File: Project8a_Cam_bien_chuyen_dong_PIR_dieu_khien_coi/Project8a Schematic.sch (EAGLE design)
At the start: 6 parts, among them U1 ARDUINOR3-BPLACE

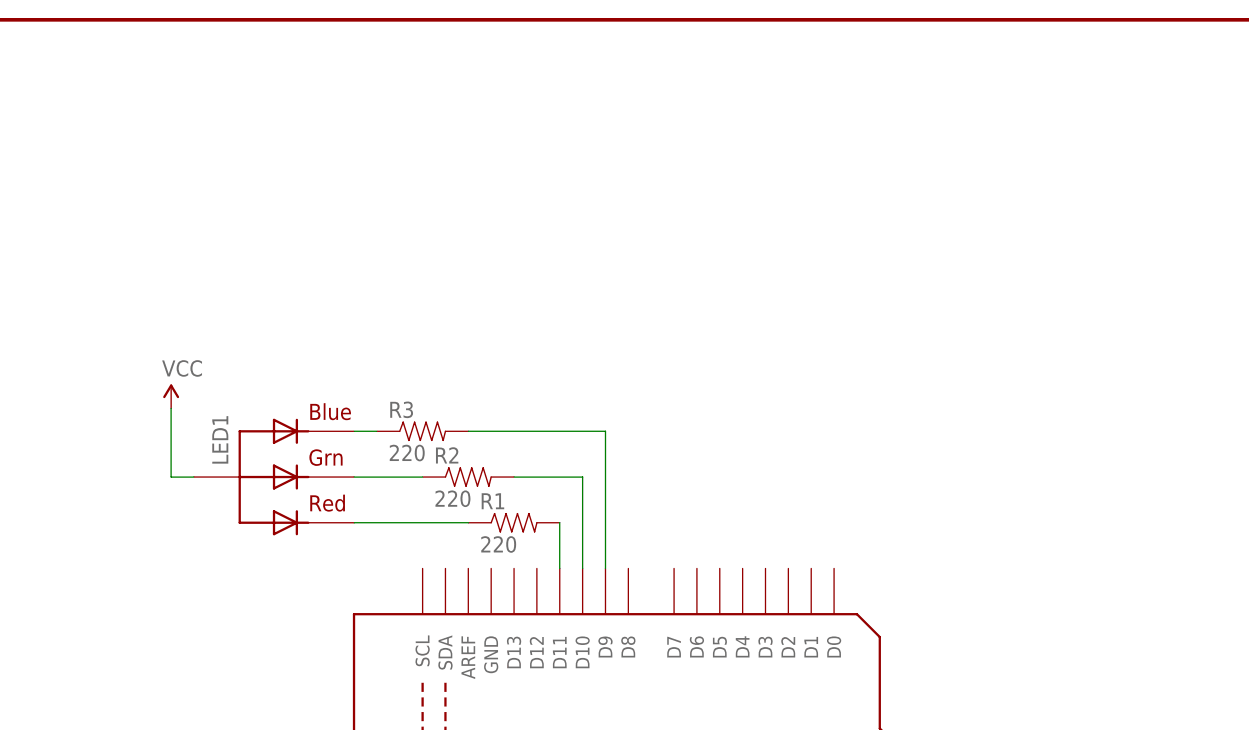
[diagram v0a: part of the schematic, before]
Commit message: Update schematic, breadboard cho nhieu projects.
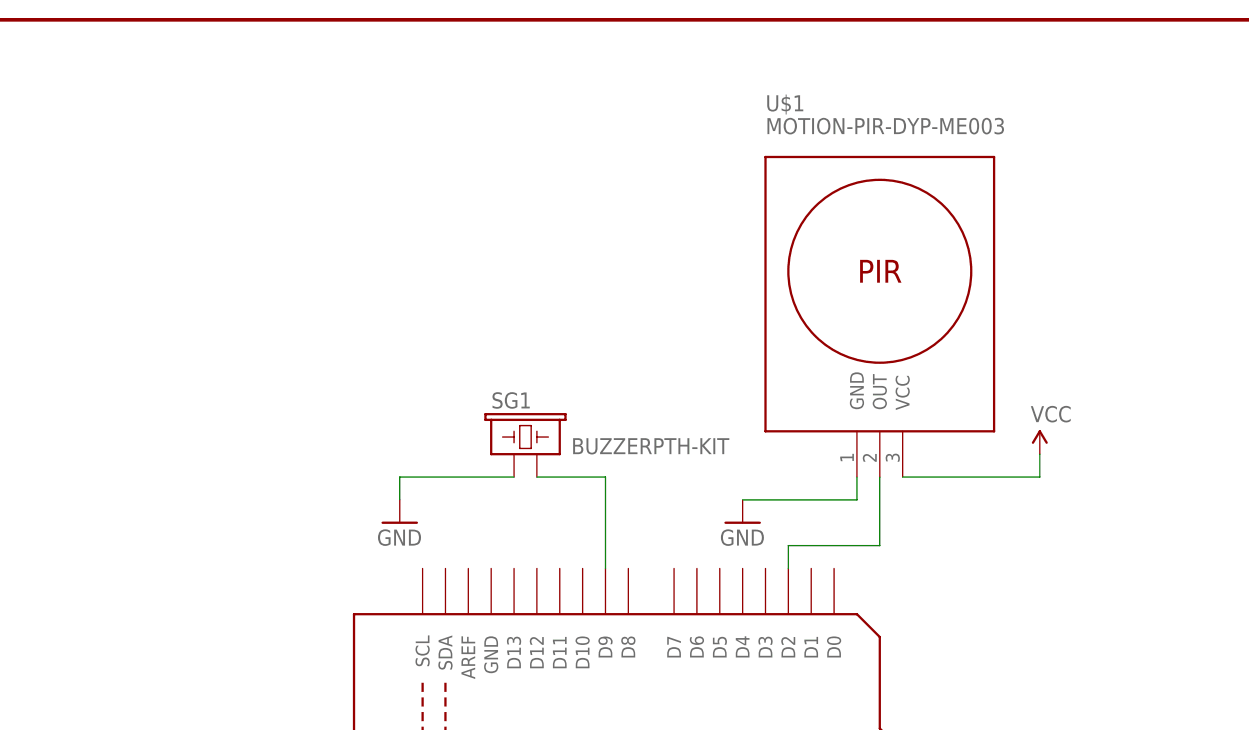
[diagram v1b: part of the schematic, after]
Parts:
- removed LED1: RGBLED_CA-5MM, adafruit:RGBLED_CA-5MM
- removed R1, R2, R3: 220, SparkFun-Passives:RESISTOR0402-RES
- added SG1: BUZZERPTH-KIT, SparkFun-Electromechanical:BUZZERPTH-KIT
- added U$1: MOTION-PIR-DYP-ME003, diy-modules:MOTION-PIR-DYP-ME003
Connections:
- removed net N$2: R2.2, U1.D10
- removed net N$4: LED1.BLUE, R3.1
- removed net N$5: LED1.GREEN, R2.1
- removed net N$6: LED1.RED, R1.1
- net GND: now also SG1.1, U$1.GND
- net N$1: now also SG1.2, U1.D9; no longer R1.2, U1.D11
- net N$3: now also U$1.OUT, U1.D2; no longer R3.2, U1.D9
- net VCC: now also U$1.VCC; no longer LED1.VCC
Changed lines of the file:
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@@
 <layer number="223" name="223bmp" color="24" fill="1" visible="no" active="no"/>
 <layer number="224" name="224bmp" color="25" fill="1" visible="no" active="no"/>
+<layer number="225" name="225bmp" color="7" fill="1" visible="yes" active="yes"/>
+<layer number="226" name="226bmp" color="7" fill="1" visible="yes" active="yes"/>
+<layer number="227" name="227bmp" color="7" fill="1" visible="yes" active="yes"/>
+<layer number="228" name="228bmp" color="7" fill="1" visible="yes" active="yes"/>
+<layer number="229" name="229bmp" color="7" fill="1" visible="yes" active="yes"/>
+<layer number="230" name="230bmp" color="7" fill="1" visible="yes" active="yes"/>
 <layer number="231" name="Eagle3D_PG1" color="7" fill="1" visible="no" active="no"/>
 <layer number="232" name="Eagle3D_PG2" color="7" fill="1" visible="no" active="no"/>
@@
 <part name="SUPPLY1" library="SparkFun-Aesthetics" deviceset="VCC" device=""/>
 <part name="GND1" library="SparkFun-Aesthetics" deviceset="GND" device=""/>
-<part name="R1" library="SparkFun-Passives" deviceset="RESISTOR" device="0402-RES" value="220"/>
+<part name="GND2" library="SparkFun-Aesthetics" deviceset="GND" device=""/>
+<part name="GND3" library="SparkFun-Aesthetics" deviceset="GND" device=""/>
+<part name="SUPPLY2" library="SparkFun-Aesthetics" deviceset="VCC" device=""/>
 <part name="FRAME1" library="SparkFun-Aesthetics" deviceset="FRAME-LETTER" device=""/>
-<part name="LED1" library="adafruit" deviceset="RGBLED_CA" device="-5MM"/>
-<part name="SUPPLY3" library="SparkFun-Aesthetics" deviceset="VCC" device=""/>
-<part name="R2" library="SparkFun-Passives" deviceset="RESISTOR" device="0402-RES" value="220"/>
-<part name="R3" library="SparkFun-Passives" deviceset="RESISTOR" device="0402-RES" value="220"/>
+<part name="U$1" library="diy-modules" deviceset="MOTION-PIR-DYP-ME003" device=""/>
+<part name="SG1" library="SparkFun-Electromechanical" deviceset="BUZZER" device="PTH-KIT"/>
 </parts>
 <sheets>
@@
 <instance part="SUPPLY1" gate="G$1" x="76.2" y="43.18" rot="R180"/>
 <instance part="GND1" gate="1" x="81.28" y="40.64"/>
-<instance part="R1" gate="G$1" x="63.5" y="114.3"/>
+<instance part="GND2" gate="1" x="50.8" y="114.3"/>
+<instance part="GND3" gate="1" x="88.9" y="114.3"/>
+<instance part="SUPPLY2" gate="G$1" x="121.92" y="121.92"/>
 <instance part="FRAME1" gate="G$1" x="-33.02" y="-15.24"/>
 <instance part="FRAME1" gate="V" x="114.3" y="-15.24"/>
-<instance part="LED1" gate="G$1" x="38.1" y="119.38"/>
-<instance part="SUPPLY3" gate="G$1" x="25.4" y="127"/>
-<instance part="R2" gate="G$1" x="58.42" y="119.38"/>
-<instance part="R3" gate="G$1" x="53.34" y="124.46"/>
+<instance part="U$1" gate="G$1" x="104.14" y="139.7"/>
+<instance part="SG1" gate="G$1" x="63.5" y="121.92"/>
 </instances>
 <busses>
@@
 </segment>
 <segment>
-<pinref part="SUPPLY3" gate="G$1" pin="VCC"/>
-<wire x1="25.4" y1="127" x2="25.4" y2="119.38" width="0.1524" layer="91"/>
-<pinref part="LED1" gate="G$1" pin="VCC"/>
-<wire x1="25.4" y1="119.38" x2="27.94" y2="119.38" width="0.1524" layer="91"/>
+<pinref part="U$1" gate="G$1" pin="VCC"/>
+<pinref part="SUPPLY2" gate="G$1" pin="VCC"/>
+<wire x1="106.68" y1="119.38" x2="121.92" y2="119.38" width="0.1524" layer="91"/>
+<wire x1="121.92" y1="119.38" x2="121.92" y2="121.92" width="0.1524" layer="91"/>
 </segment>
 </net>
@@
 <wire x1="81.28" y1="48.26" x2="81.28" y2="43.18" width="0.1524" layer="91"/>
 </segment>
-</net>
-<net name="N$1" class="0">
 <segment>
-<pinref part="U1" gate="G$1" pin="D11"/>
-<wire x1="68.58" y1="114.3" x2="68.58" y2="109.22" width="0.1524" layer="91"/>
-<pinref part="R1" gate="G$1" pin="2"/>
+<pinref part="GND3" gate="1" pin="GND"/>
+<pinref part="U$1" gate="G$1" pin="GND"/>
+<wire x1="88.9" y1="116.84" x2="101.6" y2="116.84" width="0.1524" layer="91"/>
+<wire x1="101.6" y1="116.84" x2="101.6" y2="119.38" width="0.1524" layer="91"/>
 </segment>
-</net>
-<net name="N$2" class="0">
 <segment>
-<pinref part="U1" gate="G$1" pin="D10"/>
-<wire x1="71.12" y1="119.38" x2="71.12" y2="109.22" width="0.1524" layer="91"/>
-<pinref part="R2" gate="G$1" pin="2"/>
-<wire x1="71.12" y1="119.38" x2="63.5" y2="119.38" width="0.1524" layer="91"/>
+<pinref part="SG1" gate="G$1" pin="1"/>
+<wire x1="63.5" y1="119.38" x2="50.8" y2="119.38" width="0.1524" layer="91"/>
+<pinref part="GND2" gate="1" pin="GND"/>
+<wire x1="50.8" y1="119.38" x2="50.8" y2="116.84" width="0.1524" layer="91"/>
 </segment>
 </net>
 <net name="N$3" class="0">
 <segment>
-<pinref part="U1" gate="G$1" pin="D9"/>
-<wire x1="73.66" y1="124.46" x2="73.66" y2="109.22" width="0.1524" layer="91"/>
-<pinref part="R3" gate="G$1" pin="2"/>
-<wire x1="58.42" y1="124.46" x2="73.66" y2="124.46" width="0.1524" layer="91"/>
+<pinref part="U$1" gate="G$1" pin="OUT"/>
+<wire x1="104.14" y1="119.38" x2="104.14" y2="111.76" width="0.1524" layer="91"/>
+<wire x1="104.14" y1="111.76" x2="93.98" y2="111.76" width="0.1524" layer="91"/>
+<pinref part="U1" gate="G$1" pin="D2"/>
+<wire x1="93.98" y1="111.76" x2="93.98" y2="109.22" width="0.1524" layer="91"/>
 </segment>
 </net>
-<net name="N$4" class="0">
+<net name="N$1" class="0">
 <segment>
-<pinref part="LED1" gate="G$1" pin="BLUE"/>
-<pinref part="R3" gate="G$1" pin="1"/>
-<wire x1="45.72" y1="124.46" x2="48.26" y2="124.46" width="0.1524" layer="91"/>
+<pinref part="U1" gate="G$1" pin="D9"/>
+<wire x1="73.66" y1="109.22" x2="73.66" y2="119.38" width="0.1524" layer="91"/>
+<pinref part="SG1" gate="G$1" pin="2"/>
+<wire x1="73.66" y1="119.38" x2="66.04" y2="119.38" width="0.1524" layer="91"/>
 </segment>
 </net>
-<net name="N$5" class="0">
-<segment>
-<pinref part="LED1" gate="G$1" pin="GREEN"/>
-<pinref part="R2" gate="G$1" pin="1"/>
-<wire x1="45.72" y1="119.38" x2="53.34" y2="119.38" width="0.1524" layer="91"/>
-</segment>
-</net>
-<net name="N$6" class="0">
-<segment>
-<pinref part="LED1" gate="G$1" pin="RED"/>
-<pinref part="R1" gate="G$1" pin="1"/>
-<wire x1="45.72" y1="114.3" x2="58.42" y2="114.3" width="0.1524" layer="91"/>
-</segment>
-</net>

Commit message: Thay doi schematic cua projects.
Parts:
- renumbered U$1 to U2
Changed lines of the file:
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@@
 <?xml version="1.0" encoding="utf-8"?>
 <!DOCTYPE eagle SYSTEM "eagle.dtd">
-<eagle version="7.2.0">
+<eagle version="7.3.0">
 <drawing>
 <settings>
@@
 <part name="SUPPLY2" library="SparkFun-Aesthetics" deviceset="VCC" device=""/>
 <part name="FRAME1" library="SparkFun-Aesthetics" deviceset="FRAME-LETTER" device=""/>
-<part name="U$1" library="diy-modules" deviceset="MOTION-PIR-DYP-ME003" device=""/>
+<part name="U2" library="diy-modules" deviceset="MOTION-PIR-DYP-ME003" device=""/>
 <part name="SG1" library="SparkFun-Electromechanical" deviceset="BUZZER" device="PTH-KIT"/>
 </parts>
@@
 <instance part="FRAME1" gate="G$1" x="-33.02" y="-15.24"/>
 <instance part="FRAME1" gate="V" x="114.3" y="-15.24"/>
-<instance part="U$1" gate="G$1" x="104.14" y="139.7"/>
+<instance part="U2" gate="G$1" x="104.14" y="139.7"/>
 <instance part="SG1" gate="G$1" x="63.5" y="121.92"/>
 </instances>
@@
 </segment>
 <segment>
-<pinref part="U$1" gate="G$1" pin="VCC"/>
+<pinref part="U2" gate="G$1" pin="VCC"/>
 <pinref part="SUPPLY2" gate="G$1" pin="VCC"/>
 <wire x1="106.68" y1="119.38" x2="121.92" y2="119.38" width="0.1524" layer="91"/>
@@
 <segment>
 <pinref part="GND3" gate="1" pin="GND"/>
-<pinref part="U$1" gate="G$1" pin="GND"/>
+<pinref part="U2" gate="G$1" pin="GND"/>
 <wire x1="88.9" y1="116.84" x2="101.6" y2="116.84" width="0.1524" layer="91"/>
 <wire x1="101.6" y1="116.84" x2="101.6" y2="119.38" width="0.1524" layer="91"/>
@@
 <net name="N$3" class="0">
 <segment>
-<pinref part="U$1" gate="G$1" pin="OUT"/>
+<pinref part="U2" gate="G$1" pin="OUT"/>
 <wire x1="104.14" y1="119.38" x2="104.14" y2="111.76" width="0.1524" layer="91"/>
 <wire x1="104.14" y1="111.76" x2="93.98" y2="111.76" width="0.1524" layer="91"/>
